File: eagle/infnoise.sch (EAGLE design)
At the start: 25 parts, among them SW1 NS5B1G385DFT2G, SW2 NS5B1G385DFT2G, U1 FT240XQ, X1 USBSMT-MALE

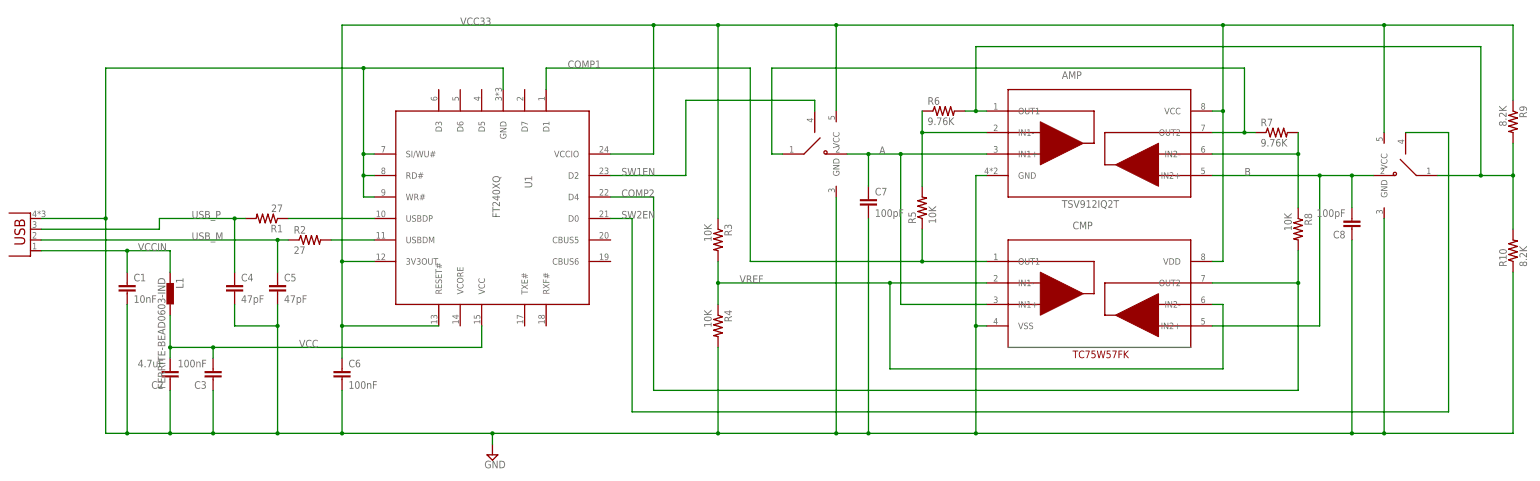
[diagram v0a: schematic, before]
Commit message: Updates to board based on fixes to breadboard
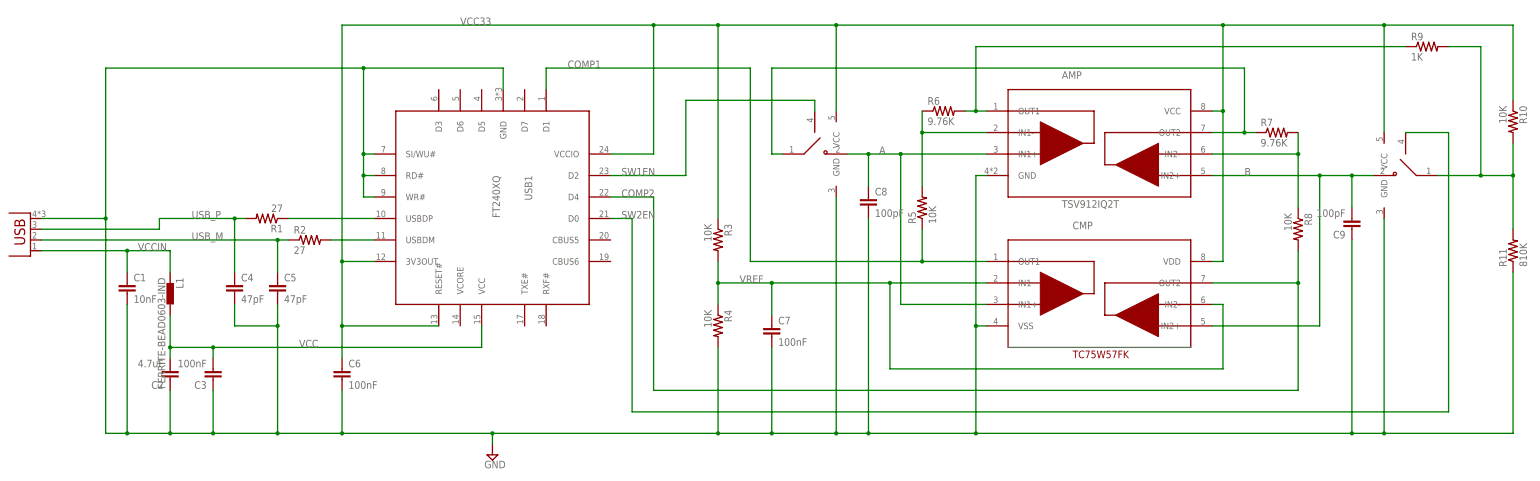
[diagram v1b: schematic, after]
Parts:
- added C9: 100pF, infnoise:CAP0603-CAP
- added R11: 810K, infnoise:RESISTOR0603-RES
- C7: value 100pF -> 100nF
- R10: value 8.2K -> 10K
- R9: value 8.2K -> 1K
- SW1, SW2: value NS5B1G385DFT2G -> MC74VHC1G66DFT1G; device infnoise:NS5B1G385DFT2G -> infnoise:MC74VHC1G66DFT1G
- renumbered U1 to USB1
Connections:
- new net N$1: AMP.OUT1, R6.2, R9.1
- net A: now also C8.1; no longer C7.1
- net AMP1OUT: now also R11.2; no longer AMP.OUT1, R6.2
- net B: now also C9.2; no longer C8.2
- net GND: now also C8.2, C9.1, R11.1; no longer C8.1, R10.1
- net VCC33: now also R10.1; no longer R9.1
- net VREF: now also C7.1
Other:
- moved on the sheet: C7, C8, R10, R9

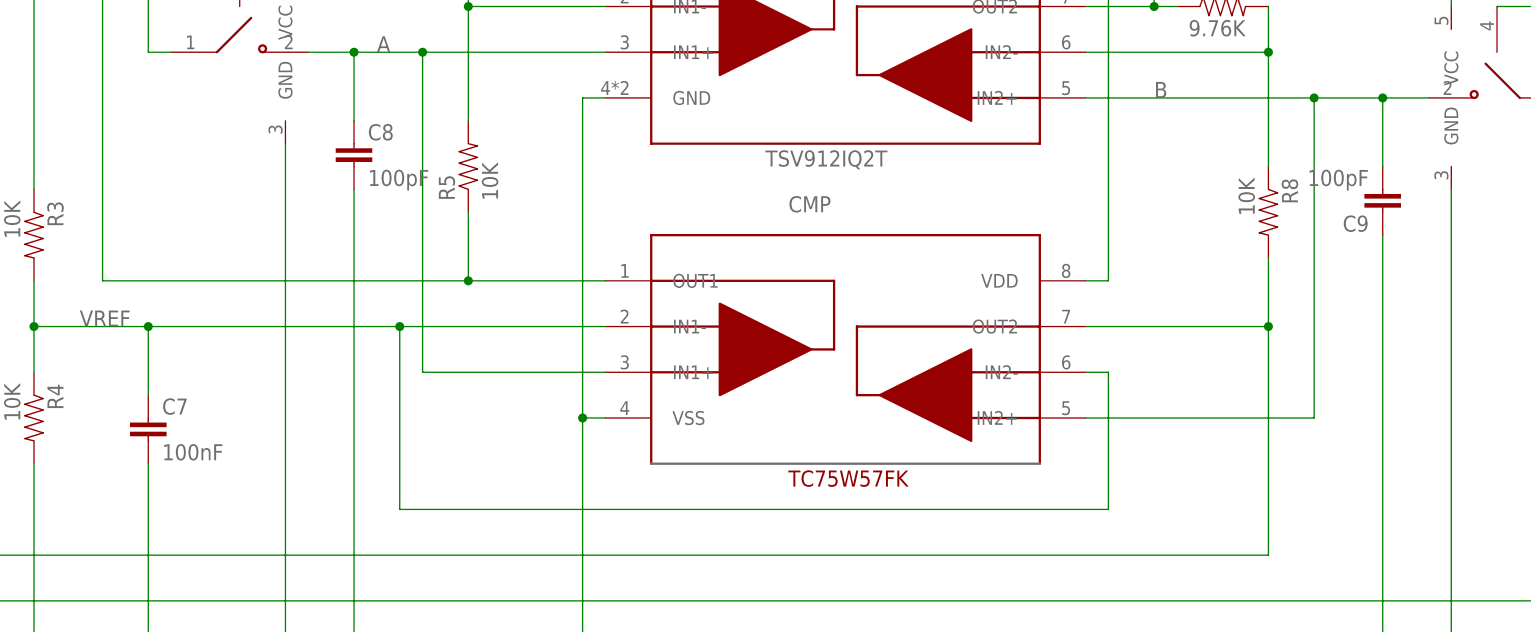
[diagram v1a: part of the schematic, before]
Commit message: Changed 100pF caps to 220pF
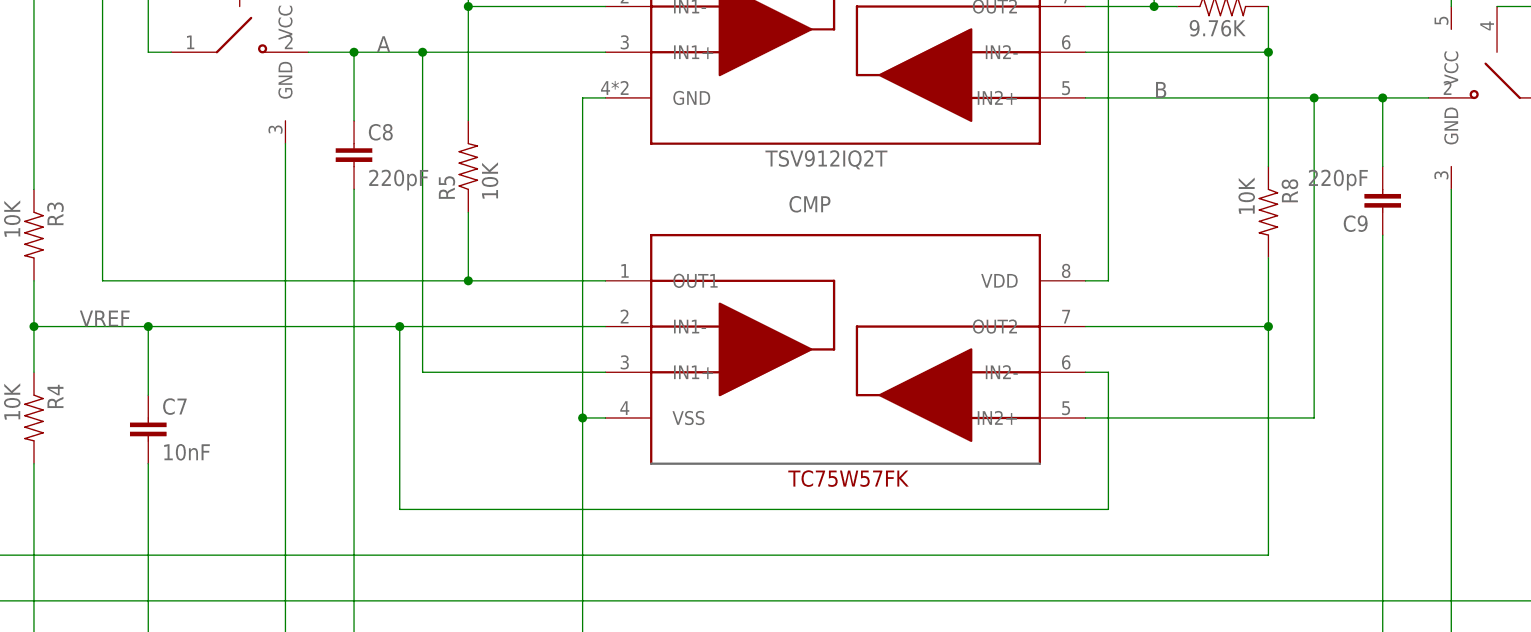
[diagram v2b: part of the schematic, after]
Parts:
- C7: value 100nF -> 10nF
- C8, C9: value 100pF -> 220pF
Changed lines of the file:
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@@
 <part name="C2" library="infnoise" deviceset="CAP" device="0603-CAP" value="4.7uF"/>
 <part name="C3" library="infnoise" deviceset="CAP" device="0603-CAP" value="100nF"/>
-<part name="C8" library="infnoise" deviceset="CAP" device="0603-CAP" value="100pF"/>
-<part name="C9" library="infnoise" deviceset="CAP" device="0603-CAP" value="100pF"/>
+<part name="C8" library="infnoise" deviceset="CAP" device="0603-CAP" value="220pF"/>
+<part name="C9" library="infnoise" deviceset="CAP" device="0603-CAP" value="220pF"/>
 <part name="C1" library="infnoise" deviceset="CAP" device="0603-CAP" value="10nF"/>
 <part name="L1" library="infnoise" deviceset="FERRITE-BEAD" device="0603-IND"/>
@@
 <part name="X1" library="infnoise" deviceset="USB" device="SMT-MALE"/>
 <part name="R9" library="infnoise" deviceset="RESISTOR" device="0603-RES" value="1K"/>
-<part name="C7" library="infnoise" deviceset="CAP" device="0603-CAP" value="100nF"/>
+<part name="C7" library="infnoise" deviceset="CAP" device="0603-CAP" value="10nF"/>
 </parts>
 <sheets>
